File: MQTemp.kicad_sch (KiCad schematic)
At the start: 8 parts, among them J1 Conn_01x02_Male, SW1 SW_DIP_x01

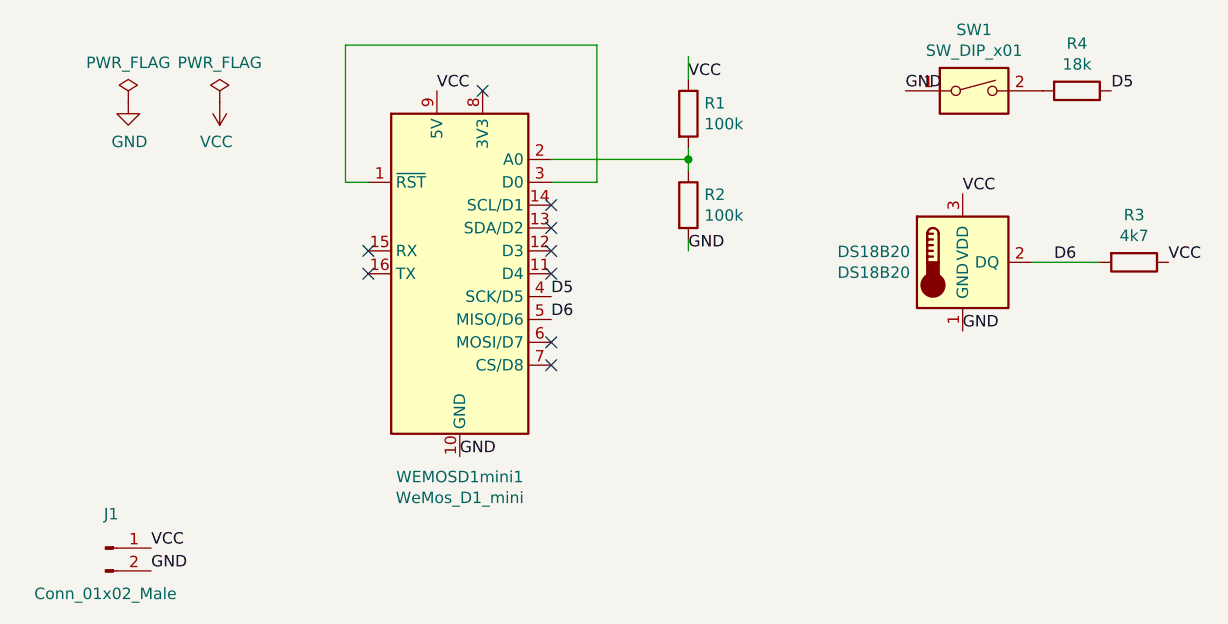
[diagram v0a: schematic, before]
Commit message: Added filled zones
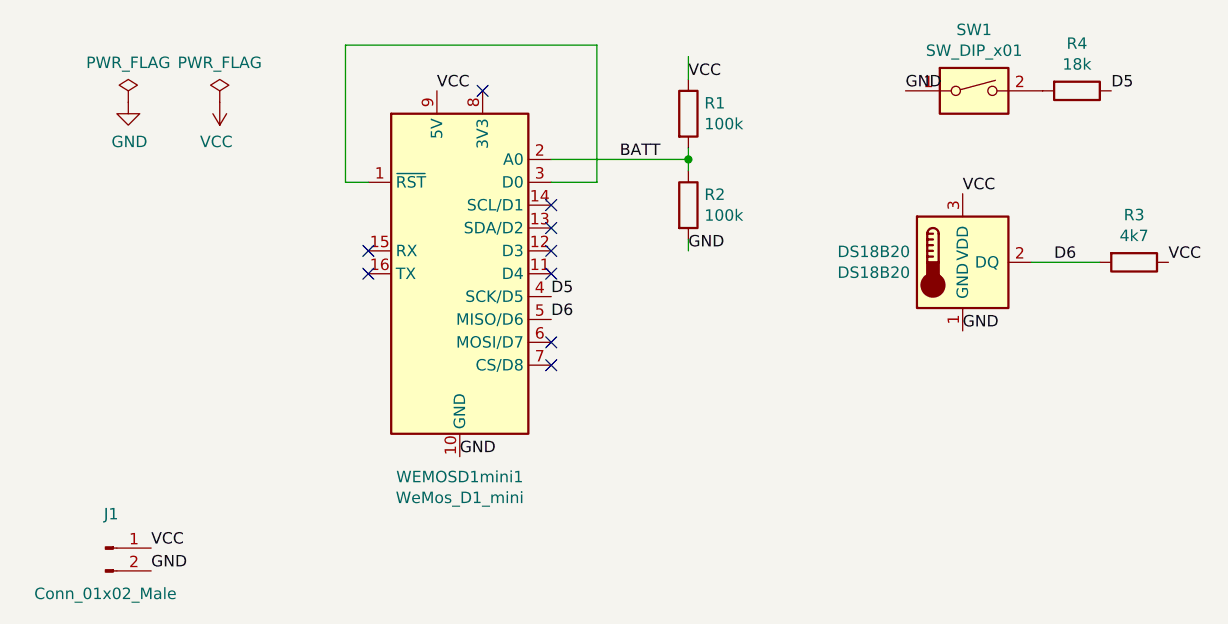
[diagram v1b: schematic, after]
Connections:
- net BATT: now reaches R1.2, R2.1, WEMOSD1mini1.2 (A0)
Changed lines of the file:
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@@
+    (effects (font (size 1.27 1.27)) (justify left bottom))
+  )
+  (label "BATT" (at 80.01 30.48 0)
     (effects (font (size 1.27 1.27)) (justify left bottom))
   )
